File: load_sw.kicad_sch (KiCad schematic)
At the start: 31 parts, among them Q3 PSMN020-100YS, U15 TPS16851VMAR, U16 LM5050-1

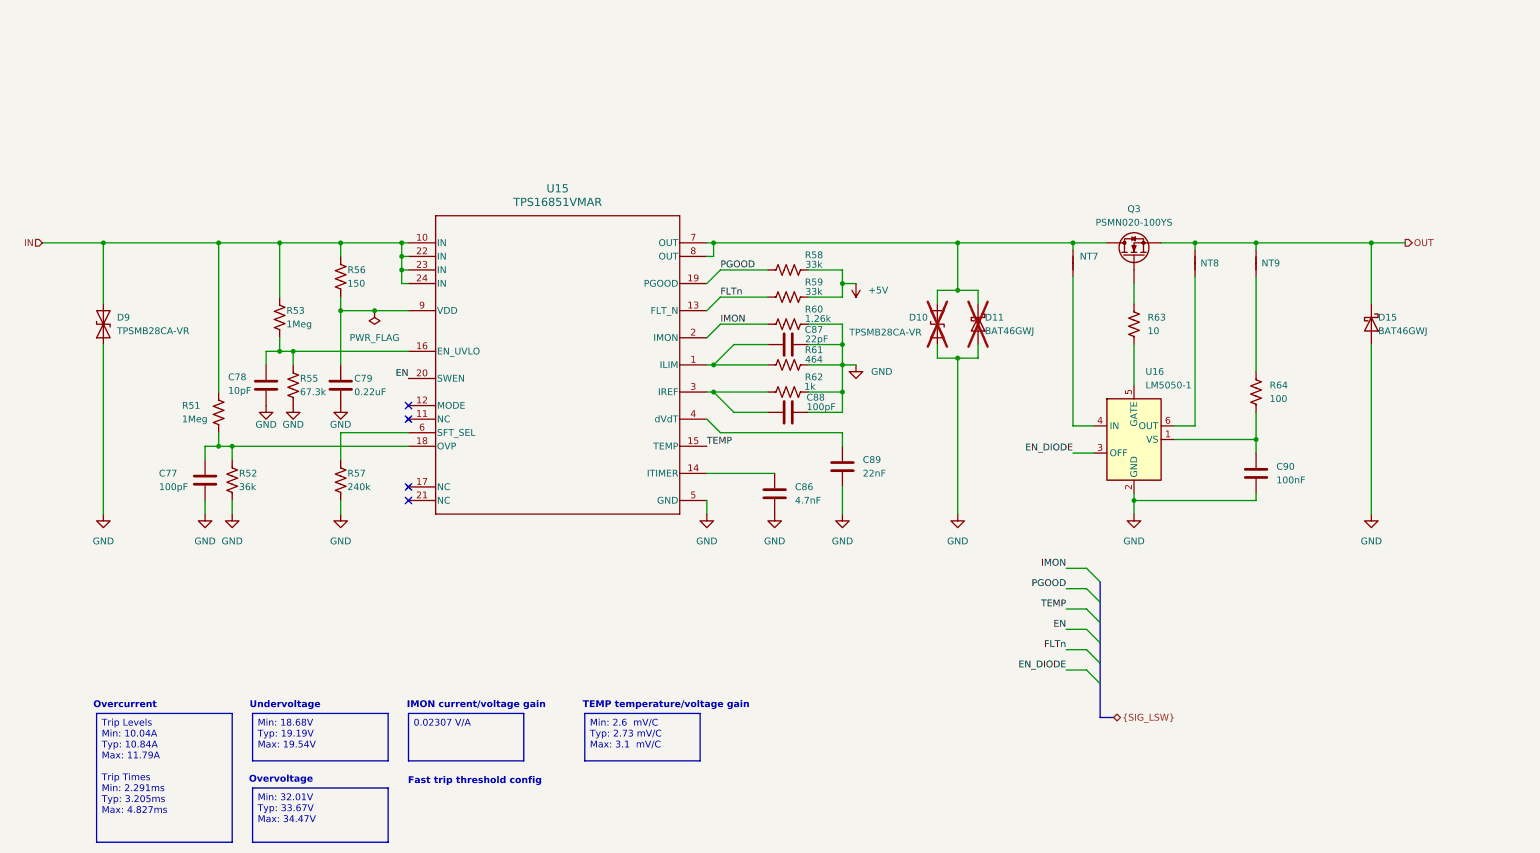
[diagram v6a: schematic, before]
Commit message: Starting bus load switch layout
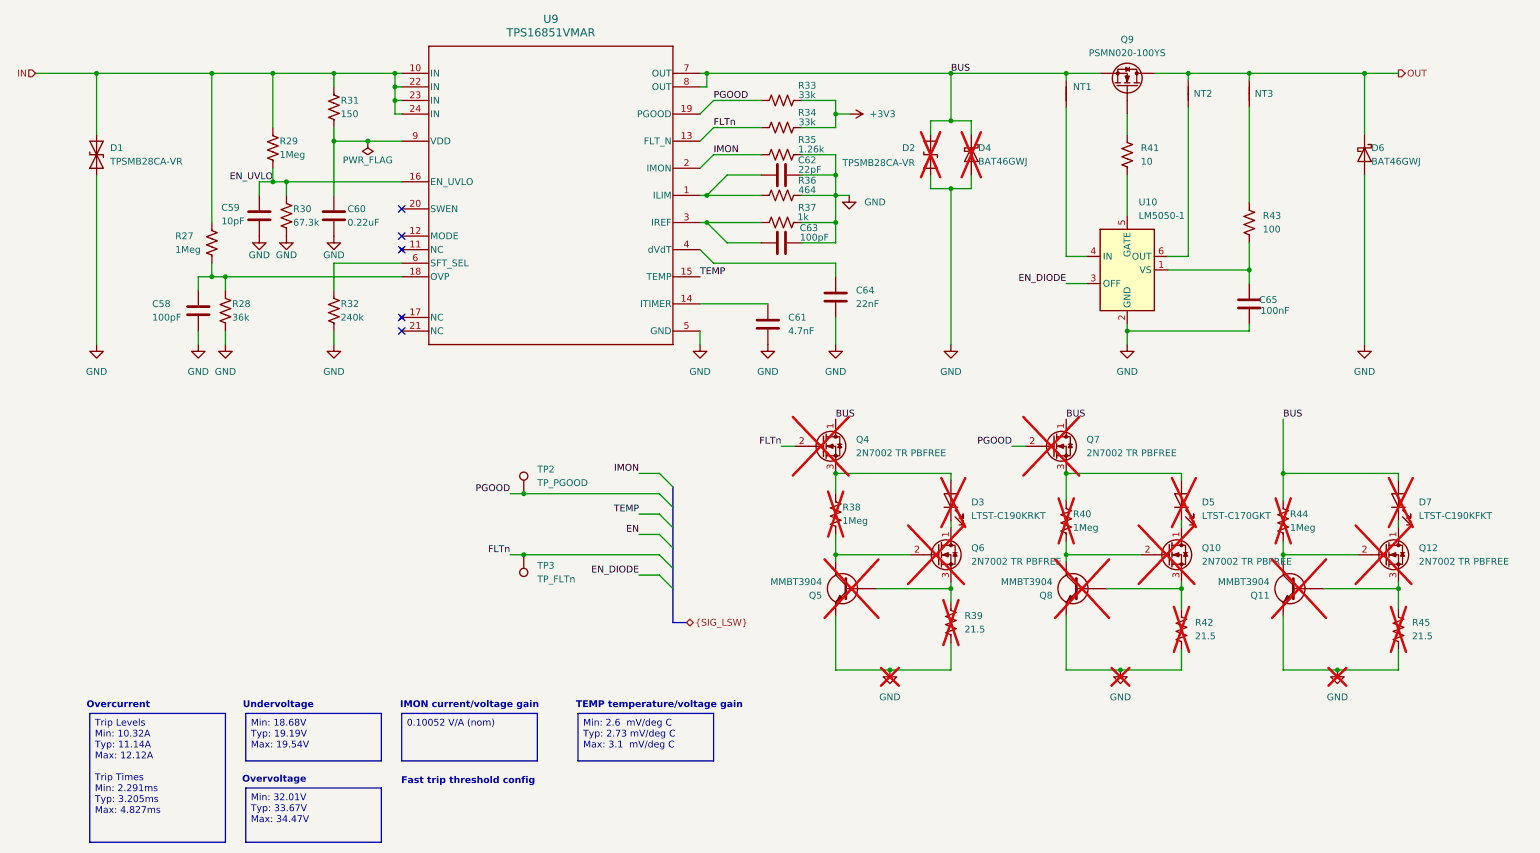
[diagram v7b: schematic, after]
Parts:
- removed C77, C88: 100pF, Capacitor_SMD:C_0603_1608Metric, symbol Device:C
- removed C78: 10pF, Capacitor_SMD:C_0603_1608Metric, symbol Device:C
- removed C79: 0.22uF, Capacitor_SMD:C_0603_1608Metric, symbol Device:C
- removed C86: 4.7nF, Resistor_SMD:R_0603_1608Metric, symbol Device:C
- removed C87: 22pF, Capacitor_SMD:C_0603_1608Metric, symbol Device:C
- removed C89: 22nF, Capacitor_SMD:C_0805_2012Metric, symbol Device:C
- removed C90: 100nF, Capacitor_SMD:C_0805_2012Metric, symbol Device:C
- removed D10, D9: TPSMB28CA-VR, Diode_SMD:D_SMB, symbol Device:D_TVS
- removed D11: BAT46GWJ, Diode_SMD:D_SOD-123, symbol Device:D_Schottky
- removed Q3: PSMN020-100YS, Package_TO_SOT_SMD:LFPAK56, symbol Device:Q_NMOS
- removed R51, R53: 1Meg, Resistor_SMD:R_0603_1608Metric, symbol Device:R_US
- removed R52: 36k, Resistor_SMD:R_0603_1608Metric, symbol Device:R_US
- removed R55: 67.3k, Resistor_SMD:R_0603_1608Metric, symbol Device:R_US
- removed R56: 150, Resistor_SMD:R_0603_1608Metric, symbol Device:R_US
- removed R57: 240k, Resistor_SMD:R_0603_1608Metric, symbol Device:R_US
- removed R58, R59: 33k, Resistor_SMD:R_0603_1608Metric, symbol Device:R_US
- removed R60: 1.26k, Resistor_SMD:R_0603_1608Metric, symbol Device:R_US
- removed R61: 464, Resistor_SMD:R_0603_1608Metric, symbol Device:R_US
- removed R62: 1k, Resistor_SMD:R_0603_1608Metric, symbol Device:R_US
- removed R63: 10, Resistor_SMD:R_1206_3216Metric, symbol Device:R_US
- removed R64: 100, Resistor_SMD:R_0603_1608Metric, symbol Device:R_US
- removed U15: TPS16851VMAR, _Power_Board:05-08-7040_ADI, symbol _TPS1685:PTPS16850VMAR
- removed U16: LM5050-1, Package_TO_SOT_SMD:TSOT-23-6, symbol Power_Management:LM5050-1
- added C58, C63: 100pF, Capacitor_SMD:C_0603_1608Metric, symbol Device:C
- added C59: 10pF, Capacitor_SMD:C_0603_1608Metric, symbol Device:C
- added C60: 0.22uF, Capacitor_SMD:C_0603_1608Metric, symbol Device:C
- added C61: 4.7nF, Resistor_SMD:R_0603_1608Metric, symbol Device:C
- added C62: 22pF, Capacitor_SMD:C_0603_1608Metric, symbol Device:C
- added C64: 22nF, Capacitor_SMD:C_0805_2012Metric, symbol Device:C
- added C65: 100nF, Capacitor_SMD:C_0603_1608Metric, symbol Device:C
- added D1, D2: TPSMB28CA-VR, Diode_SMD:D_SMB, symbol Device:D_TVS
- added D3: LTST-C190KRKT, LED_SMD:LED_0603_1608Metric, symbol Device:LED
- added D4: BAT46GWJ, Diode_SMD:D_SOD-123, symbol Device:D_Schottky
- added D5: LTST-C170GKT, LED_SMD:LED_0805_2012Metric, symbol Device:LED
- added D7: LTST-C190KFKT, LED_SMD:LED_0603_1608Metric, symbol Device:LED
- added Q10, Q12, Q4, Q6, Q7: 2N7002 TR PBFREE, Package_TO_SOT_SMD:TSOT-23, symbol Transistor_FET:Q_NMOS_DGS
- added Q11, Q5, Q8: MMBT3904, Package_TO_SOT_SMD:TSOT-23, symbol Device:Q_NPN
- added Q9: PSMN020-100YS, Package_TO_SOT_SMD:LFPAK56, symbol Device:Q_NMOS
- added R27, R29, R38, R40, R44: 1Meg, Resistor_SMD:R_0603_1608Metric, symbol Device:R_US
- added R28: 36k, Resistor_SMD:R_0603_1608Metric, symbol Device:R_US
- added R30: 67.3k, Resistor_SMD:R_0603_1608Metric, symbol Device:R_US
- added R31: 150, Resistor_SMD:R_0603_1608Metric, symbol Device:R_US
- added R32: 240k, Resistor_SMD:R_0603_1608Metric, symbol Device:R_US
- added R33, R34: 33k, Resistor_SMD:R_0603_1608Metric, symbol Device:R_US
- added R35: 1.26k, Resistor_SMD:R_0603_1608Metric, symbol Device:R_US
- added R36: 464, Resistor_SMD:R_0603_1608Metric, symbol Device:R_US
- added R37: 1k, Resistor_SMD:R_0603_1608Metric, symbol Device:R_US
- added R39, R42, R45: 21.5, Resistor_SMD:R_0603_1608Metric, symbol Device:R_US
- added R41: 10, Resistor_SMD:R_1206_3216Metric, symbol Device:R_US
- added R43: 100, Resistor_SMD:R_0603_1608Metric, symbol Device:R_US
- added TP2: TP_PGOOD, TestPoint:TestPoint_Plated_Hole_D5.0mm, symbol Connector:TestPoint
- added TP3: TP_FLTn, TestPoint:TestPoint_Plated_Hole_D5.0mm, symbol Connector:TestPoint
- added U10: LM5050-1, Package_TO_SOT_SMD:TSOT-23-6, symbol Power_Management:LM5050-1
- added U9: TPS16851VMAR, _PowerBoard:VMA0023A-MFG, symbol _TPS1685:PTPS16850VMAR
- D6: renamed from D15; Supplier_1 Price @ Qty 0.19000 -> 1; Supplier_1 Unit Price 1 -> 0.19000
- NT1: renamed from NT7; footprint (none) -> NetTie:NetTie-2_SMD_Pad0.5mm
- NT2: renamed from NT8; footprint (none) -> NetTie:NetTie-2_SMD_Pad0.5mm
- NT3: renamed from NT9; footprint (none) -> NetTie:NetTie-2_SMD_Pad0.5mm
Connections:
- net EN_DIODE: now also U10.3 (OFF)
- net FLTn: now also Q4.2 (G), R34.1, TP3.1, U9.13 (FLT_N)
- net GND: now also C58.2, C59.2, C60.2, C61.2, C62.2, C63.2, C64.2, C65.2, D1.1 (A1), D2.1 (A1), D4.2 (A), Q11.E, Q5.E, Q8.E, R28.2, R30.2, R32.2, R35.2, R36.2, R37.2, R39.2, R42.2, R45.2, U10.2 (GND), U9.5 (GND)
- net IMON: now also R35.1, U9.2 (IMON)
- net IN: now also D1.2 (A2), R27.1, R29.1, R31.1, U9.10 (IN), U9.22 (IN), U9.23 (IN), U9.24 (IN)
- net OUT: now also Q9.D
- net PGOOD: now also Q7.2 (G), R33.1, TP2.1, U9.19 (PGOOD)
- net TEMP: now also U9.15 (TEMP)
- net at NT1.1: now also U10.4 (IN)
- net BUS: now reaches NT1.2
- net BUS: now also D2.2 (A2), D4.1 (K), D7.2 (A), Q4.1 (D), Q7.1 (D), Q9.S, R44.1, U9.7 (OUT), U9.8 (OUT)
- net at NT3.1: now also R43.2
- net at NT2.1: now also U10.6 (OUT)
- new net: D5.2 (A), Q7.3 (S), R40.1
- new net: Q10.2 (G), Q8.C, R40.2
- new net: C63.1, R37.1, U9.3 (IREF)
- new net: D5.1 (K), Q10.1 (D)
- new net: Q10.3 (S), Q8.B, R42.1
- new net: C60.1, R31.2, U9.9 (VDD)
- new net: C58.1, R27.2, R28.1, U9.18 (OVP)
- new net: C64.1, U9.4 (dVdT)
- new net: C65.1, R43.1, U10.1 (VS)
- new net: R32.1, U9.6 (SFT_SEL)
- new net: D7.1 (K), Q12.1 (D)
- new net: Q11.C, Q12.2 (G), R44.2
- new net: Q11.B, Q12.3 (S), R45.1
- new net: Q5.B, Q6.3 (S), R39.1
- new net: Q9.G, R41.1
- new net: D3.2 (A), Q4.3 (S), R38.1
- new net: Q5.C, Q6.2 (G), R38.2
- new net: D3.1 (K), Q6.1 (D)
- new net: C62.1, R36.1, U9.1 (ILIM)
- new net: R41.2, U10.5 (GATE)
- new net: C61.1, U9.14 (ITIMER)
- new net +3V3: R33.2, R34.2
- new net EN_UVLO: C59.1, R29.2, R30.1, U9.16 (EN_UVLO)
- no-connect marks 4 -> 5
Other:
- moved on the sheet: D6, NT1, NT2, NT3

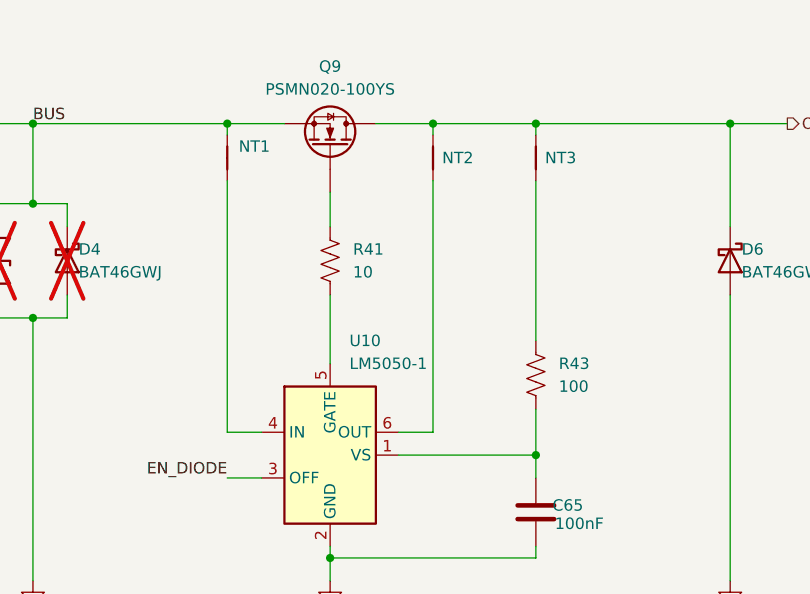
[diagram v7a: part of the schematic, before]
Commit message: Laying out NavLight LSW & fixing up bus LSW
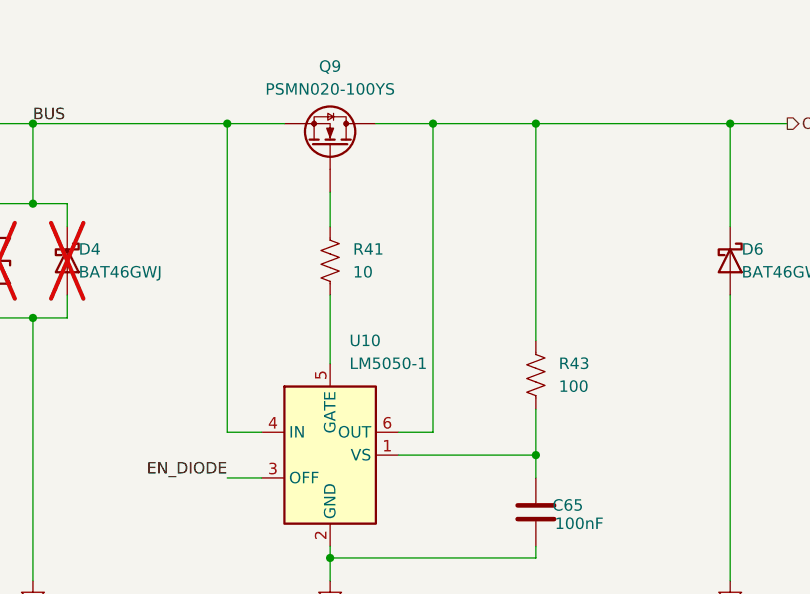
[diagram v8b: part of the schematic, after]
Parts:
- removed NT1, NT2, NT3: NetTie_2, NetTie:NetTie-2_SMD_Pad0.5mm, symbol Device:NetTie_2
- Q9: footprint Package_TO_SOT_SMD:LFPAK56 -> _PowerBoard:LFPAK56_1
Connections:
- net BUS: now also Q9.3 (S), U10.4 (IN); no longer Q9.S
- net OUT: now also Q9.1 (D), R43.2, U10.6 (OUT); no longer Q9.D
- net at R41.1: now also Q9.2 (G); no longer Q9.G
